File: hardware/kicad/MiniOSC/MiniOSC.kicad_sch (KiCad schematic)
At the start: 68 parts, among them J1 SYNC_IN, J10 FM_IN, J11 PWM_CV, J12 TRI_OUT, J13 SAW_OUT, J14 PULSE_OUT, J2 Conn_01x10_Pin, J9 VOCT_IN, Q3 BC848, Q4 BC858, SW1 SW_DPDT_x2, U1 40106, U2 TL074, U3 TL074

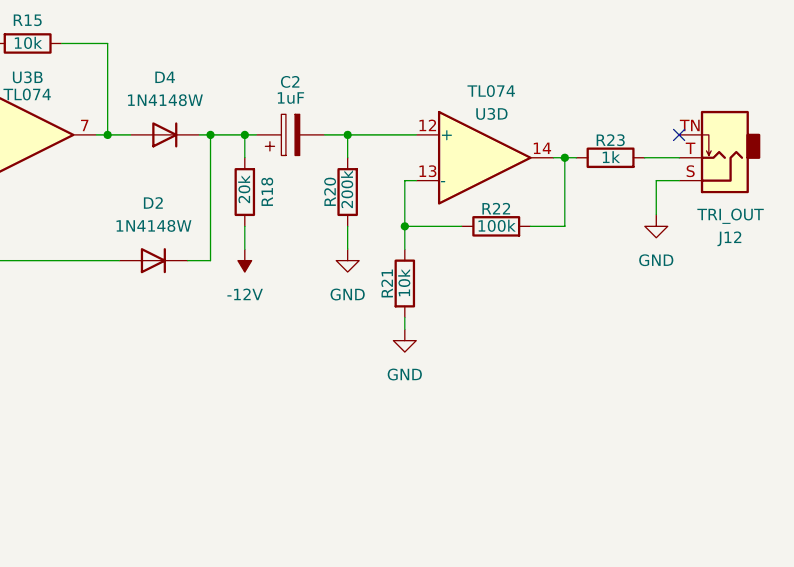
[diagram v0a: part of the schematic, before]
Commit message: Updated R21 value
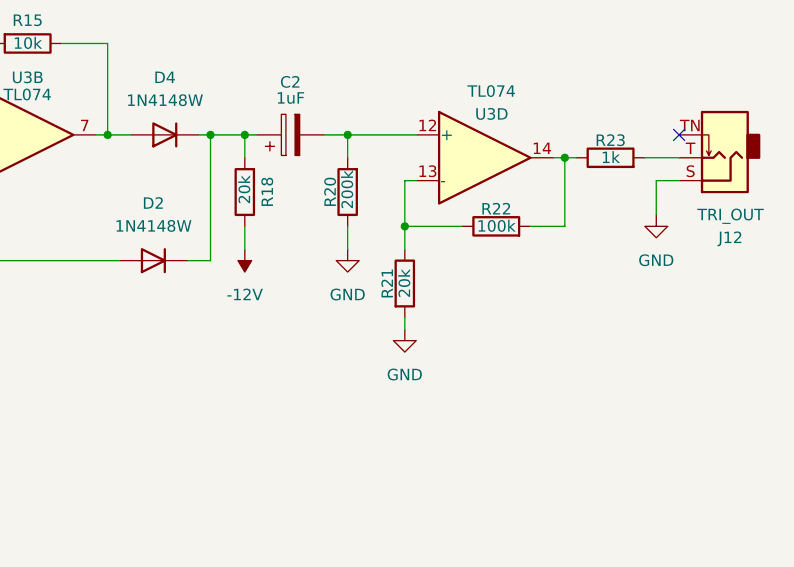
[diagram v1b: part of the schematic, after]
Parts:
- R21: value 10k -> 20k
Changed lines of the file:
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@@
 			)
 		)
-		(property "Value" "10k"
+		(property "Value" "20k"
 			(at 237.49 149.86 90)
 			(effects

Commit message: Updated changelog
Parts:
- R14: value 33k -> 67k
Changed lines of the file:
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@@
 			)
 		)
-		(property "Value" "33k"
+		(property "Value" "67k"
 			(at 191.77 71.12 90)
 			(effects

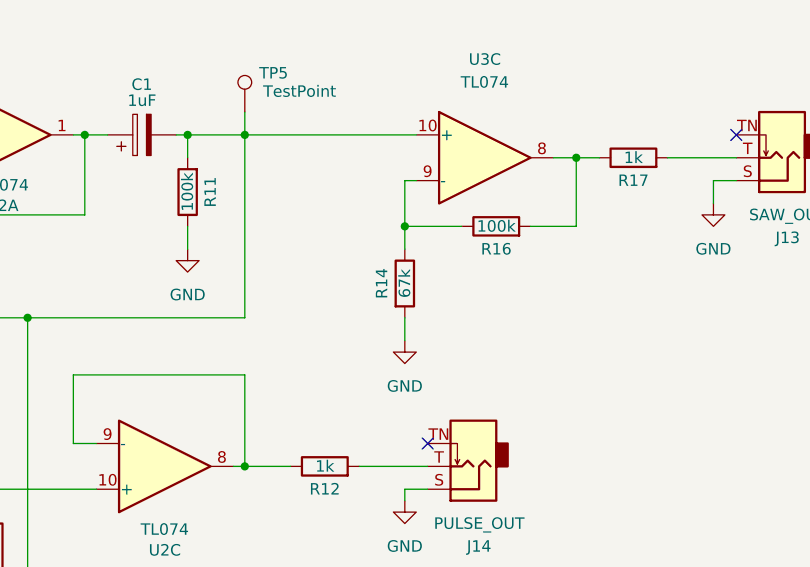
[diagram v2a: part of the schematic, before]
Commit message: Fixed typo on R14 value
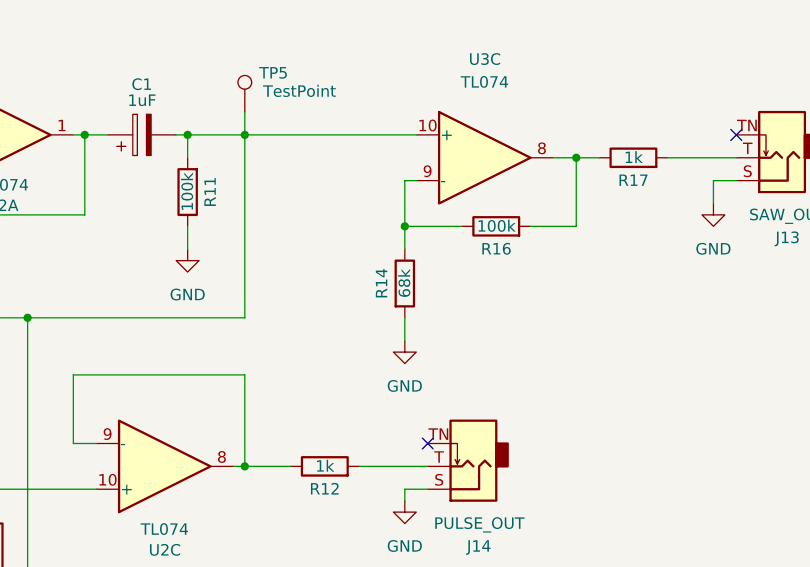
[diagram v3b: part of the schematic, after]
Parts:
- R14: value 67k -> 68k
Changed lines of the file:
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@@
 			)
 		)
-		(property "Value" "67k"
+		(property "Value" "68k"
 			(at 191.77 71.12 90)
 			(effects

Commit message: Added manufacture parts numbers to BOM
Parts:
- C1, C2: Manufacturer (none) -> TAIYO YUDEN; Part # (none) -> UMK107AB7105KA-T
- C10, C9: Manufacturer (none) -> Panasonic; Part # (none) -> EEE-FT1V220AR
- C3, C4, C5, C6, C7: Manufacturer (none) -> YAGEO; Part # (none) -> CC0603JRX7R9BB104
- C8: Manufacturer (none) -> Vishay / Vitramon; Part # (none) -> VJ0603Y681KXAAC; URL https://mou.sr/3zee3wG -> https://mou.sr/4goVMgC
- D1, D2, D3, D4: Manufacturer (none) -> Panjit; Part # (none) -> 1N4148W_R2_00001
- FM_AMT1: Manufacturer (none) -> ALPHA; Part # (none) -> RV09AF-40-20K-B1M
- J1, J10, J11, J12, J13, J14, J9: Manufacturer (none) -> Tayda Electronics; Part # (none) -> PJ-3001F 3.5mm Mono Phone Jack
- J2: Manufacturer (none) -> XKB Connectivity; Part # (none) -> X9555WV-2X05-6TV01
- PULSE_WIDTH1, TUNING_COARSE1: Manufacturer (none) -> Tayda Electronics; Part # (none) -> RV9312NO-OS15A00-B100K-060
- PWM_AMT1, TUNING_FINE1: Manufacturer (none) -> ALPHA; Part # (none) -> RV09AF-40-20K-B100K
- Q3: Manufacturer (none) -> onsemi; Part # (none) -> BC848ALT1G
- Q4: Manufacturer (none) -> onsemi; Part # (none) -> BC858CLT3G
- R1, R10, R11, R16, R2, R22, R4, R7: Manufacturer (none) -> YAGEO; Part # (none) -> RC0603FR-07100KL
- R12, R17, R19, R23: Manufacturer (none) -> YAGEO; Part # (none) -> RC0603FR-071KL
- R13, R15, R21, R9: Manufacturer (none) -> YAGEO; Part # (none) -> AC0603FR-0710KL
- R14: Manufacturer (none) -> YAGEO; Part # (none) -> RC0603FR-0768KL; URL https://mou.sr/4ebt4y6 -> https://mou.sr/3ToI2ZD
- R18, R8: Manufacturer (none) -> YAGEO; Part # (none) -> RC0603FR-0720KL
- R20: Manufacturer (none) -> Bourns; Part # (none) -> CR0603-FX-2003ELF
- R24: Manufacturer (none) -> YAGEO; Part # (none) -> RC0603FR-0768KL
- R3, R6: Manufacturer (none) -> YAGEO; Part # (none) -> RC0603FR-071ML
- R5: Manufacturer (none) -> YAGEO; Part # (none) -> RC0603FR-071K5L
- SCALE1: Manufacturer (none) -> ALPHA; Part # (none) -> 3296W-1-102LF
- SW1: Manufacturer (none) -> DAIER; Part # (none) -> PB-22E27-ROHS
- TH1, TH2, TH3, TH4: Manufacturer (none) -> Vishay / BC Components; Part # (none) -> NTCS0603E3103JLT
- U1: Manufacturer (none) -> Texas Instruments; Part # (none) -> CD40106BM96G4
- U2, U3: Manufacturer (none) -> STMicroelectronics; Part # (none) -> TL074ACDT

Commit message: Added links to PCBWay, updated bom
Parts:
- C8: value 680pF -> 2.2nF; URL https://mou.sr/4goVMgC -> https://mou.sr/3zee3wG
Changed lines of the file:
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@@
 			)
 		)
-		(property "Value" "680pF"
+		(property "Value" "2.2nF"
 			(at 122.301 59.563 0)
 			(effects
@@
 			)
 		)
-		(property "URL" "https://mou.sr/4goVMgC"
+		(property "URL" "https://mou.sr/3zee3wG"
 			(at 119.38 58.42 0)
 			(effects

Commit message: Fixed v2.1 BOM
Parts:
- R21: Part # AC0603FR-0710KL -> RC0603FR-0720KL; URL https://mou.sr/3MINYsI -> https://mou.sr/3z5b9KJ
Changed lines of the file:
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@@
 			)
 		)
-		(property "URL" "https://mou.sr/3MINYsI"
+		(property "URL" "https://mou.sr/3z5b9KJ"
 			(at 237.49 149.86 0)
 			(effects
@@
 			)
 		)
-		(property "Part #" "AC0603FR-0710KL"
+		(property "Part #" "RC0603FR-0720KL"
 			(at 237.49 149.86 0)
 			(effects
